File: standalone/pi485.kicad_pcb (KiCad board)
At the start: 2 copper layers, 63 x 46 mm, 29 parts, among them J1 RS485, P1 Rasperry Pi, P2 PWR, P3 TERM, P4 RO, Q1 2N3904, Q2 2N3904, Q3 2N3904, Q4 2N3906, U1 NE555, U2 MAX485

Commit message: 1.1.1 schematics, trace plots, etc.
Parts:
- added C4: 10nF, Capacitors_THT:C_Rect_L4_W2.5_P2.5, F.Cu at (59.3, 20.6)
- added R12: 10k, Resistors_THT:Resistor_Horizontal_RM10mm, F.Cu at (34.6, 33.4)
- moved P3 2.54 mm to (23.8, 25.1)
- moved R5 1.55 mm to (28.9, 33.4)
- moved C3 0.12 mm to (54.3, 23.1)
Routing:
- net GND: track 184.1 -> 195.2 mm
- net Net-(R12-Pad2): track 11.4 -> 22.2 mm
- net Net-(J1-Pad1): track 33.5 -> 39.7 mm
- net Net-(P3-Pad1): track 4.67 -> 5.87 mm
- net Net-(J1-Pad2): track 34.4 -> 35.4 mm
- net Net-(C1-Pad2): track 163.0 -> 162.1 mm
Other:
- board text added: "Pi485 Rev 1.1.1"
- board text removed: "Pi485 Rev 1.1.0"

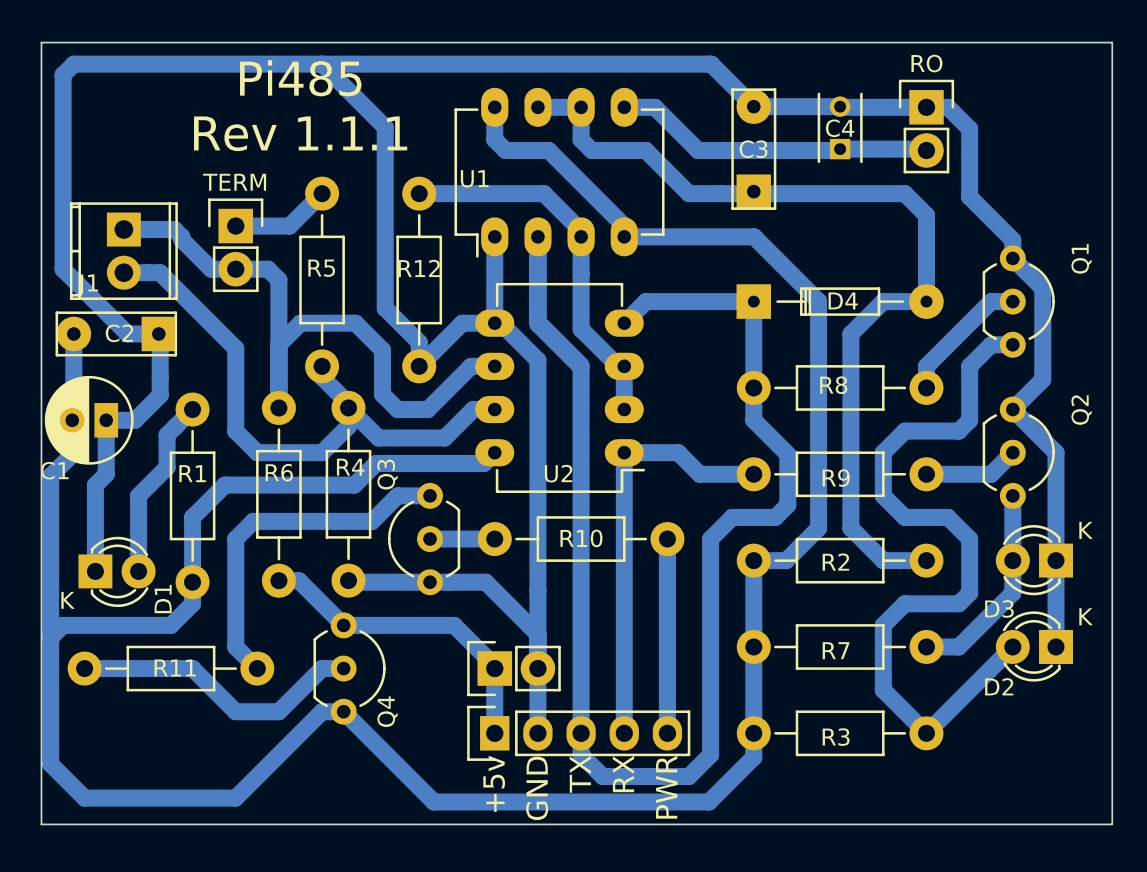
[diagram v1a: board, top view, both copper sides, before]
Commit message: Updates for jumpered biasing on standalone boards. The silly bearer modules you can just unsolder the biasing resistors if it becomes an issue. I should probably add jumpering for that too, but at this point, I just don't much care. A slight modification to those silly SMT boards really isn't that hard...
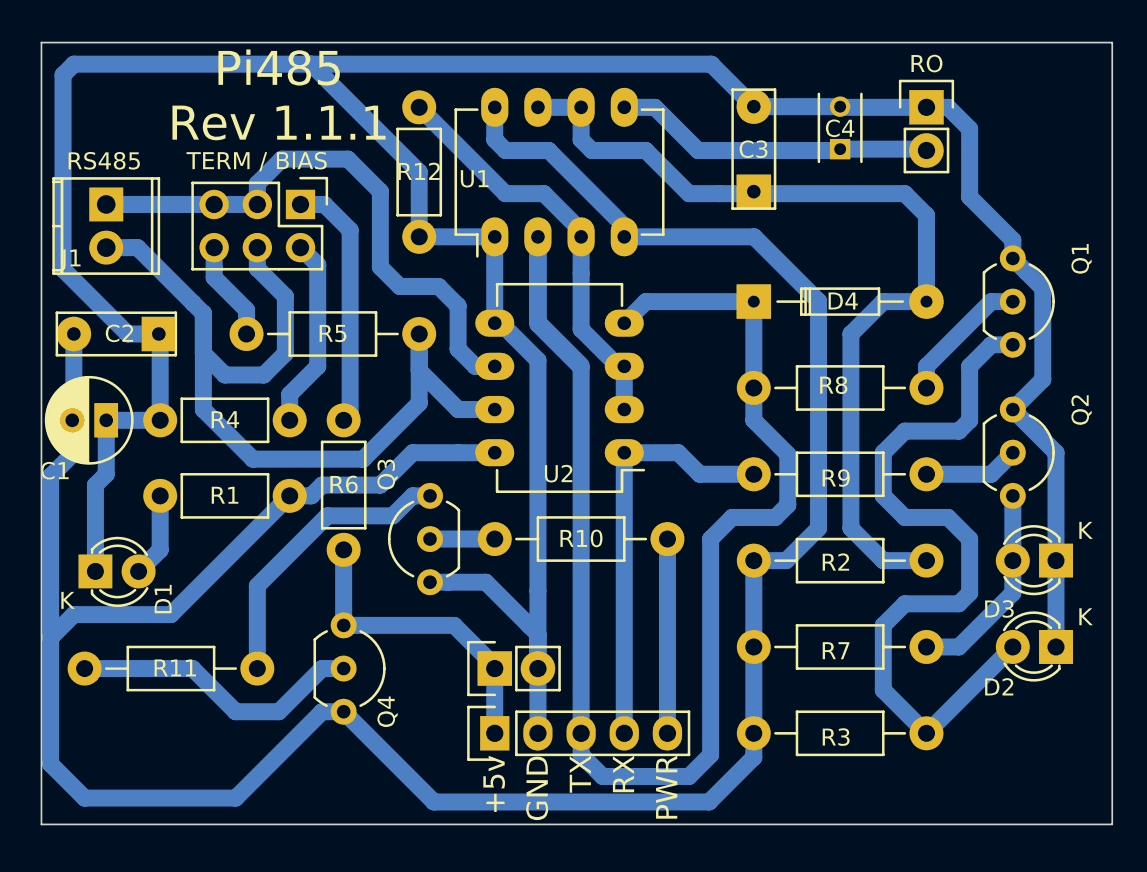
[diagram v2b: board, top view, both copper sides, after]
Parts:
- P3: value TERM -> TERM / BIAS; footprint Pin_Headers:Pin_Header_Straight_1x02 -> Pin_Headers:Pin_Header_Straight_2x03
- R1, R12, R4, R6: footprint Resistors_THT:Resistor_Horizontal_RM10mm -> Resistors_THT:Resistor_Horizontal_RM7mm
- moved R4 14.5 mm to (19.3, 36.6), turned to 0 degrees
- moved R12 7.62 mm to (34.6, 25.8)
- moved R5 6.02 mm to (34.6, 31.5), turned to 180 degrees
- moved R1 5.43 mm to (19.3, 41.0), turned to 0 degrees
- moved P3 4.02 mm to (27.6, 23.9), turned to 270 degrees
- moved R6 3.88 mm to (30.1, 36.6)
- moved J1 1.80 mm to (16.2, 23.9)
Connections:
- P3 pad 2: Net-(J1-Pad1) -> Net-(P3-Pad2)
- R4 pad 2: Net-(J1-Pad2) -> Net-(P3-Pad2)
- R5 pad 2: Net-(P3-Pad1) -> Net-(P3-Pad6)
- R6 pad 1: Net-(J1-Pad1) -> Net-(P3-Pad1)
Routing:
- net Net-(J1-Pad2): track 35.4 -> 55.0 mm
- net GND: track 195.2 -> 182.5 mm
- net Net-(P3-Pad2): track 0.00 -> 11.3 mm
- net Net-(P3-Pad1): track 5.87 -> 14.9 mm
- net Net-(J1-Pad1): track 39.7 -> 33.8 mm
- net Net-(D1-Pad2): track 10.8 -> 4.97 mm
- net Net-(P3-Pad6): track 0.00 -> 5.87 mm
- net Net-(Q3-Pad3): track 20.6 -> 17.2 mm
- net Net-(C1-Pad2): track 162.1 -> 159.0 mm
- net Net-(R12-Pad2): track 22.2 -> 24.3 mm
